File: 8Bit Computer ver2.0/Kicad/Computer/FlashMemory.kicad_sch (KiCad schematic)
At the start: 56 parts, among them IC198 DS1100Z-20+, IC199 SN74AHC74DR, IC200 SN74ABT245BDWR, IC201 SN74ABT245BDWR, IC202 SN74ABT245BDWR, IC203 SN74ABT245BDWR, IC204 SN74ABT245BDWR, IC205 M29F800FT55N3E2, IC206 SN74ABT245BDWR, IC207 M29F800FT55N3E2, IC208 SN74ABT245BDWR, IC209 SN74ABT245BDWR, IC210 SN74ABT245BDWR, IC211 SN74ABT245BDWR, IC212 SN74ABT245BDWR, IC213 SN74ABT245BDWR, IC214 SN74ABT245BDWR, IC215 SN74ABT245BDWR, J35 Conn_02x25_Odd_Even, J36 Conn_02x25_Odd_Even

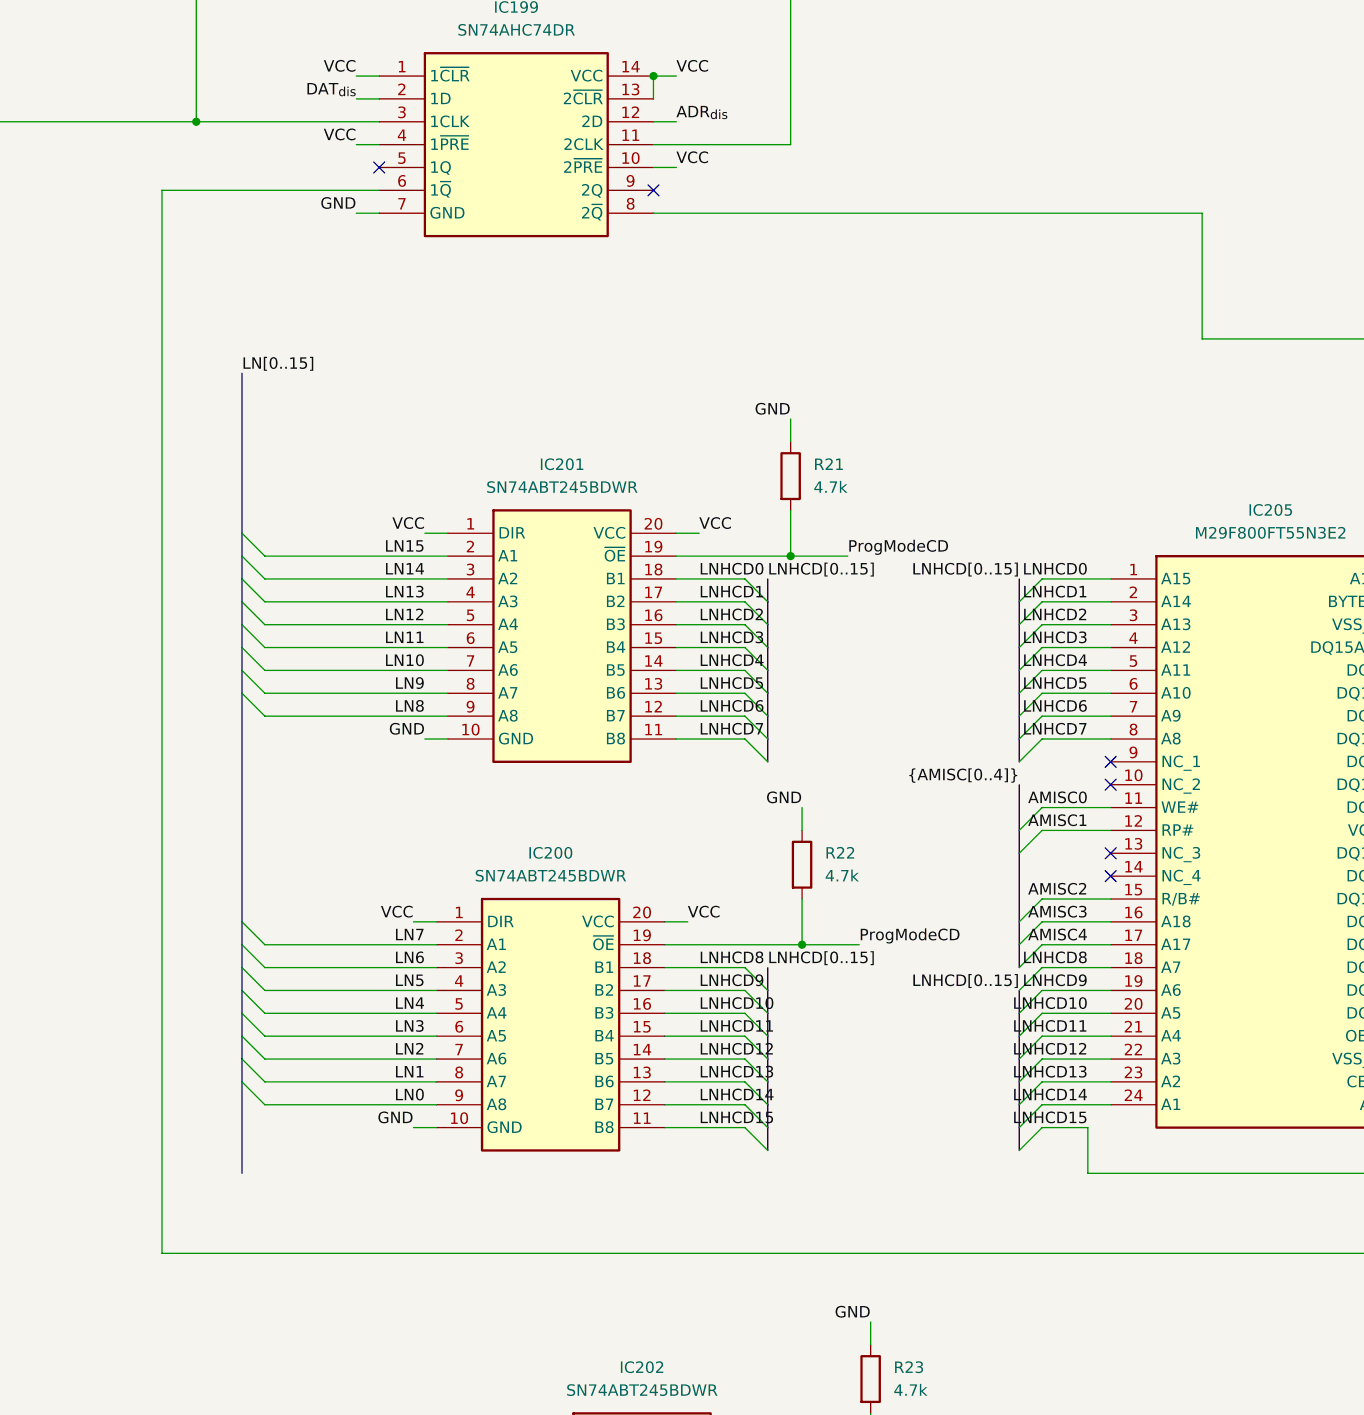
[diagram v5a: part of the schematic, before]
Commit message: updated T76 software, Kicad bugs
changed the inverting outs of IC199 to non inverting
changed Pin of CMD decoder IC237 0x2A from GND to VCC (pin5)
deleted diode d30
changed silkscreen of the Clock gen mux from 0 1 555 to 1 0 555 and buttonclk from 1 0 to 0 1
changed the DS1100-150+ of the edge detector to an or gate SN74HCS32
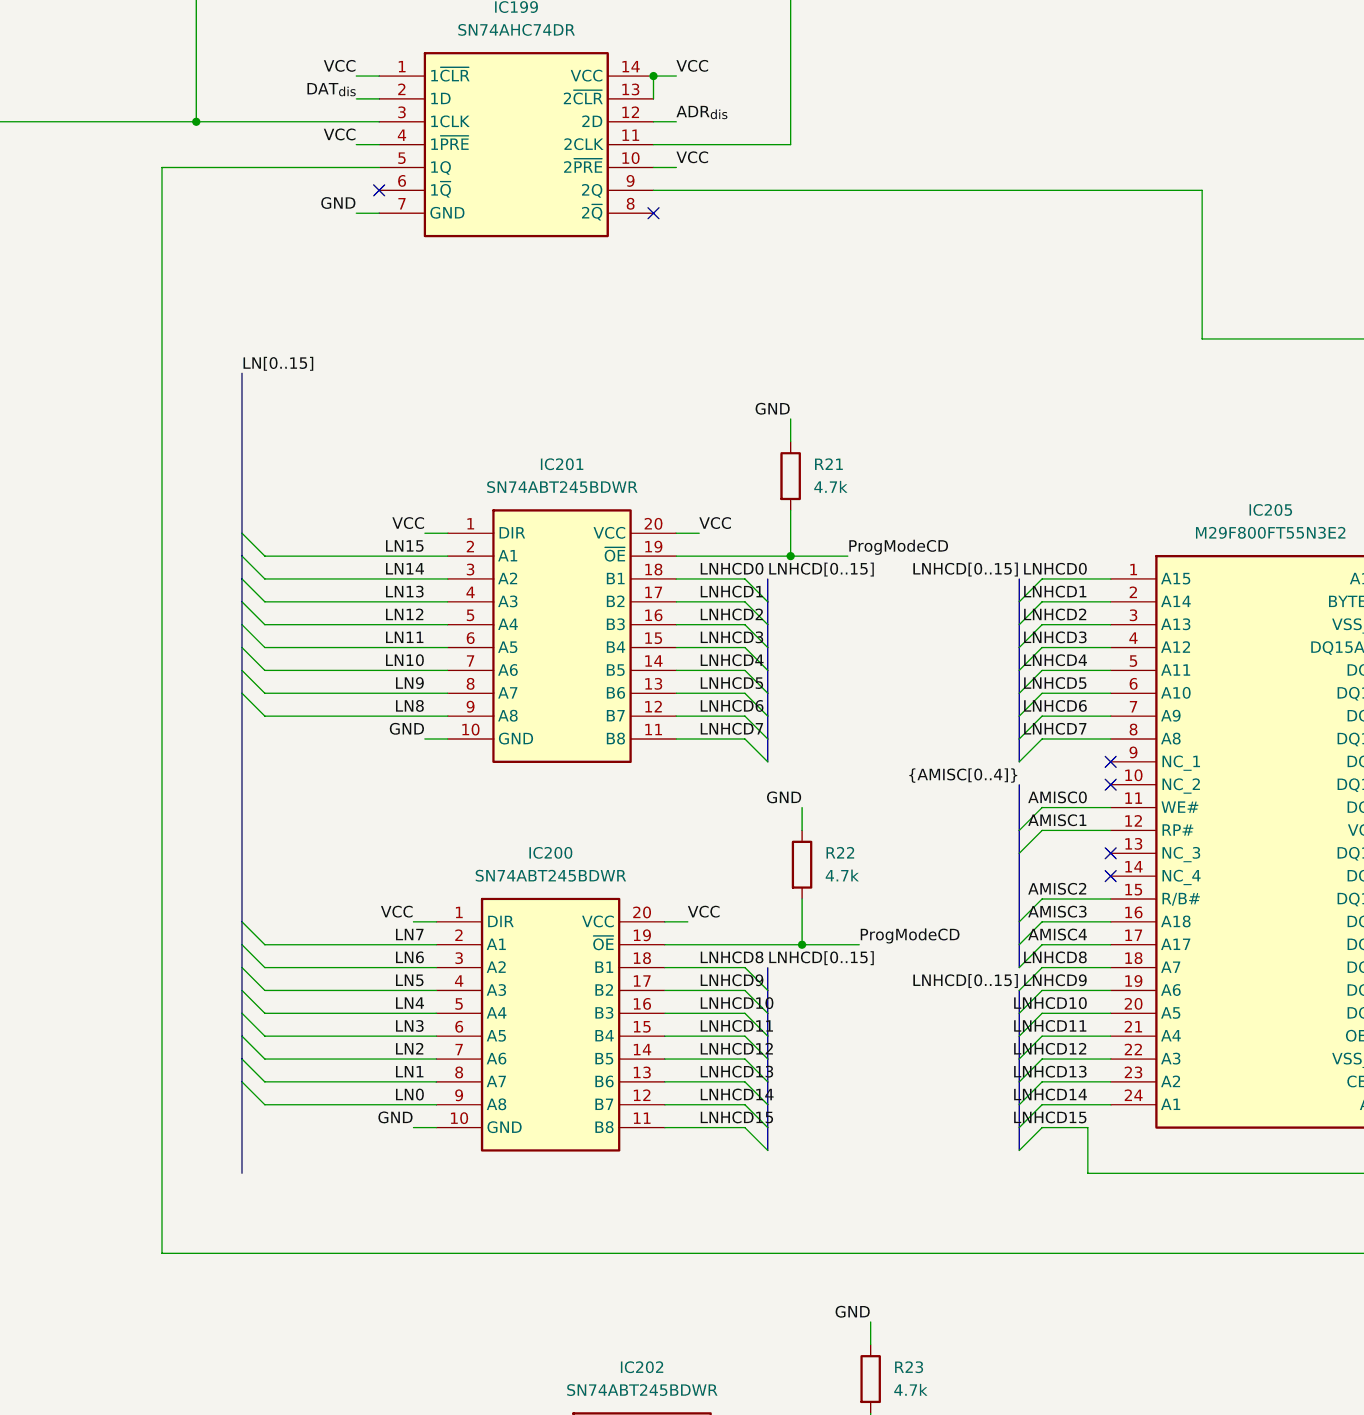
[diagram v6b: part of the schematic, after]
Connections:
- net at IC214.19 (~{OE}), IC215.19 (~{OE}): now also IC199.9 (2Q); no longer IC199.8 (2~{Q})
- net at IC199.5 (1Q): now also IC212.19 (~{OE})
- net at IC199.6 (1~{Q}): no longer IC212.19 (~{OE})
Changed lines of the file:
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@@
 	)
 	(no_connect
-		(at 234.95 312.42)
-	)
-	(no_connect
 		(at 288.29 113.03)
 	)
@@
 	)
 	(no_connect
+		(at 204.47 312.42)
+	)
+	(no_connect
 		(at 443.23 100.33)
 	)
@@
 	)
 	(no_connect
-		(at 368.3 306.07)
+		(at 234.95 314.96)
 	)
 	(no_connect
-		(at 179.07 265.43)
+		(at 368.3 306.07)
 	)
 	(no_connect
-		(at 204.47 309.88)
+		(at 179.07 265.43)
 	)
 	(no_connect
@@
 	(wire
 		(pts
-			(xy 204.47 312.42) (xy 180.34 312.42)
-		)
-		(stroke
-			(width 0)
-			(type default)
-		)
-	)
-	(wire
-		(pts
 			(xy 363.22 474.98) (xy 375.92 474.98)
 		)
@@
 	(wire
 		(pts
+			(xy 180.34 309.88) (xy 204.47 309.88)
+		)
+		(stroke
+			(width 0)
+			(type default)
+		)
+	)
+	(wire
+		(pts
 			(xy 485.14 407.67) (xy 500.38 407.67)
 		)
@@
 	(wire
 		(pts
-			(xy 180.34 312.42) (xy 180.34 430.53)
+			(xy 180.34 309.88) (xy 180.34 430.53)
 		)
 		(stroke
@@
 	(wire
 		(pts
-			(xy 295.91 314.96) (xy 295.91 328.93)
+			(xy 295.91 312.42) (xy 295.91 328.93)
 		)
 		(stroke
@@
 	(wire
 		(pts
-			(xy 234.95 314.96) (xy 295.91 314.96)
+			(xy 234.95 312.42) (xy 295.91 312.42)
 		)
 		(stroke

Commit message: Kicad
fixed some design errors(dat dis DistShiftreg, wrong cmd pins)
added description to every CMD for better debug, use CTRL+f and use option "Whole words only" to search e.g. inc
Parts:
- added C327, C328: 100nF, Capacitor_SMD:C_1206_3216Metric_Pad1.33x1.80mm_HandSolder, symbol Device:C
- added R176, R177: 4.7k, Resistor_SMD:R_1206_3216Metric_Pad1.30x1.75mm_HandSolder, symbol Device:R
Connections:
- net AMISC1: now also IC202.17 (B2)
- net CMISC1: now also IC206.17 (B2)
- net GND: now also C327.1, C328.1
- net VCC: now also C327.2, C328.2, R176.1, R177.1
- net at IC206.3 (A2): now also R176.2
- net at IC202.3 (A2): now also R177.2
- no-connect marks 34 -> 30

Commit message: fixes
fixed timing for dat to adr register
added a new short test programme for dat to adr register
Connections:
- net ADR_{dis}: now also IC214.19 (~{OE}), IC215.19 (~{OE}); no longer IC199.12 (2D)
- net VCC: now also IC199.11 (2CLK), IC199.12 (2D)
- net at IC198.3 (TAP_4), IC199.3 (1CLK): no longer IC199.11 (2CLK)
- now unconnected: IC199.9 (2Q)
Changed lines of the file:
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@@
 	)
 	(junction
-		(at 613.41 245.11)
-		(diameter 0)
-		(color 0 0 0 0)
-	)
-	(junction
 		(at 363.22 481.33)
 		(diameter 0)
@@
 	)
 	(junction
-		(at 184.15 304.8)
-		(diameter 0)
-		(color 0 0 0 0)
-	)
-	(junction
 		(at 411.48 363.22)
 		(diameter 0)
@@
 		)
 	)
-	(wire
-		(pts
-			(xy 250.19 307.34) (xy 234.95 307.34)
-		)
-		(stroke
-			(width 0)
-			(type default)
-		)
-	)
 	(bus
 		(pts
@@
 	(wire
 		(pts
-			(xy 184.15 304.8) (xy 204.47 304.8)
+			(xy 137.16 304.8) (xy 204.47 304.8)
 		)
 		(stroke
@@
 	(wire
 		(pts
-			(xy 295.91 312.42) (xy 295.91 328.93)
-		)
-		(stroke
-			(width 0)
-			(type default)
-		)
-	)
-	(wire
-		(pts
 			(xy 335.28 115.57) (xy 335.28 95.25)
 		)
@@
 		)
 	)
-	(wire
-		(pts
-			(xy 234.95 304.8) (xy 237.49 304.8)
-		)
-		(stroke
-			(width 0)
-			(type default)
-		)
-	)
 	(bus
 		(pts
@@
 	(wire
 		(pts
-			(xy 613.41 290.83) (xy 613.41 245.11)
-		)
-		(stroke
-			(width 0)
-			(type default)
-		)
-	)
-	(wire
-		(pts
 			(xy 271.78 194.31) (xy 284.48 194.31)
 		)
@@
 	(wire
 		(pts
-			(xy 184.15 304.8) (xy 184.15 287.02)
-		)
-		(stroke
-			(width 0)
-			(type default)
-		)
-	)
-	(wire
-		(pts
 			(xy 405.13 224.79) (xy 422.91 224.79)
 		)
@@
 		)
 	)
-	(wire
-		(pts
-			(xy 510.54 328.93) (xy 510.54 290.83)
-		)
-		(stroke
-			(width 0)
-			(type default)
-		)
-	)
-	(wire
-		(pts
-			(xy 234.95 312.42) (xy 295.91 312.42)
-		)
-		(stroke
-			(width 0)
-			(type default)
-		)
-	)
 	(bus
 		(pts
@@
 	(wire
 		(pts
-			(xy 510.54 290.83) (xy 613.41 290.83)
-		)
-		(stroke
-			(width 0)
-			(type default)
-		)
-	)
-	(wire
-		(pts
 			(xy 300.99 88.9) (xy 300.99 100.33)
 		)
@@
 	(wire
 		(pts
+			(xy 234.95 307.34) (xy 237.49 307.34)
+		)
+		(stroke
+			(width 0)
+			(type default)
+		)
+	)
+	(wire
+		(pts
 			(xy 191.77 355.6) (xy 212.09 355.6)
 		)
@@
 	(wire
 		(pts
-			(xy 184.15 287.02) (xy 250.19 287.02)
-		)
-		(stroke
-			(width 0)
-			(type default)
-		)
-	)
-	(wire
-		(pts
 			(xy 321.31 467.36) (xy 335.28 467.36)
 		)
@@
 	(wire
 		(pts
-			(xy 137.16 304.8) (xy 184.15 304.8)
-		)
-		(stroke
-			(width 0)
-			(type default)
-		)
-	)
-	(wire
-		(pts
 			(xy 369.57 207.01) (xy 353.06 207.01)
 		)
@@
 	(wire
 		(pts
+			(xy 234.95 304.8) (xy 237.49 304.8)
+		)
+		(stroke
+			(width 0)
+			(type default)
+		)
+	)
+	(wire
+		(pts
 			(xy 332.74 363.22) (xy 321.31 363.22)
 		)
@@
 		)
 	)
-	(wire
-		(pts
-			(xy 295.91 328.93) (xy 510.54 328.93)
-		)
-		(stroke
-			(width 0)
-			(type default)
-		)
-	)
 	(bus
 		(pts
@@
 	(wire
 		(pts
-			(xy 250.19 287.02) (xy 250.19 307.34)
-		)
-		(stroke
-			(width 0)
-			(type default)
-		)
-	)
-	(wire
-		(pts
 			(xy 485.14 422.91) (xy 500.38 422.91)
 		)
@@
 		)
 	)
+	(label "VCC"
+		(at 237.49 304.8 0)
+		(effects
+			(font
+				(size 1.27 1.27)
+			)
+			(justify left bottom)
+		)
+	)
 	(label "LNHADR10"
 		(at 274.32 245.11 0)
@@
 		)
 	)
+	(label "ADR_{dis}"
+		(at 621.03 205.74 0)
+		(effects
+			(font
+				(size 1.27 1.27)
+			)
+			(justify left bottom)
+		)
+	)
 	(label "HDATCMD13"
 		(at 441.96 422.91 0)
@@
 		)
 	)
-	(label "ADR_{dis}"
-		(at 237.49 304.8 0)
-		(effects
-			(font
-				(size 1.27 1.27)
-			)
-			(justify left bottom)
-		)
-	)
 	(label "LNHADR4"
 		(at 367.03 214.63 180)
@@
 		(effects
 			(font
+				(size 1.27 1.27)
+			)
+			(justify left bottom)
+		)
+	)
+	(label "VCC"
+		(at 237.49 307.34 0)
+		(effects
+			(font
